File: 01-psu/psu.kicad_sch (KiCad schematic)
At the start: 32 parts, among them IC1 ISOLATED_DC-DC_CONV, J1 Barrel_Jack_Switch, J10 Conn_02x08_Odd_Even, J11 Conn_02x08_Odd_Even, J12 Conn_01x03, J13 Conn_01x03, J14 Conn_01x03, J2 Conn_02x08_Odd_Even, J3 Conn_02x08_Odd_Even, J4 Conn_02x08_Odd_Even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

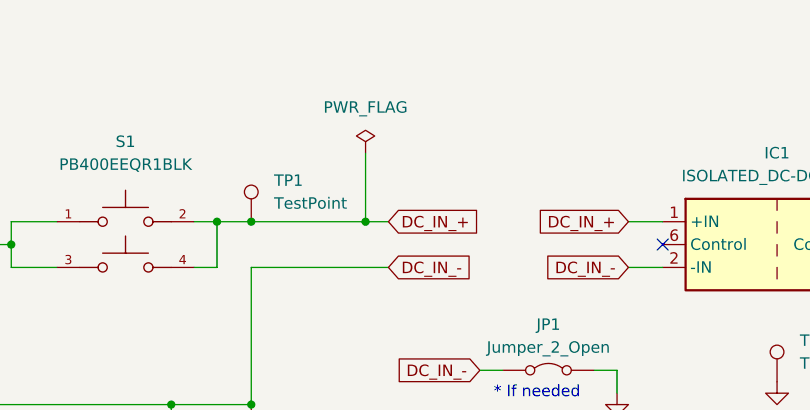
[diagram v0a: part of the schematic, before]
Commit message: Added protection diode and terminal to PSU
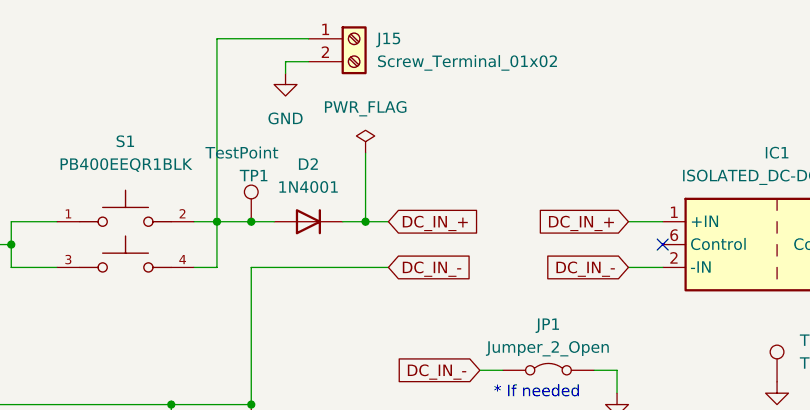
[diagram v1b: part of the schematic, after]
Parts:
- added D2: 1N4001, Diode_THT:D_DO-41_SOD81_P7.62mm_Horizontal, symbol Device:D
- added J15: Screw_Terminal_01x02, TerminalBlock_Altech:Altech_AK100_1x02_P5.00mm, symbol Connector:Screw_Terminal_01x02
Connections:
- net DC_IN_+: now also D2.1 (K); no longer S1.2, S1.4, TP1.1
- net GND: now also J15.2 (Pin_2)
- new net: D2.2 (A), J15.1 (Pin_1), S1.2, S1.4, TP1.1
